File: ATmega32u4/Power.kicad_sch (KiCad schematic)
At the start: 6 parts, among them U1 AMS1117-3.3

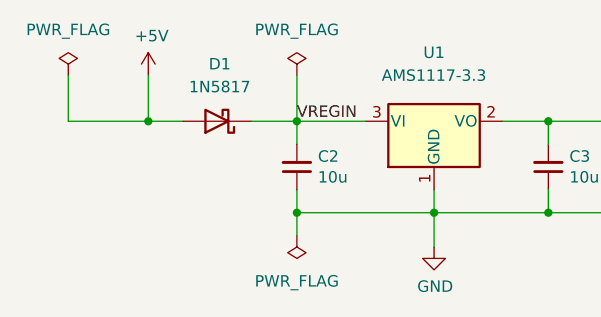
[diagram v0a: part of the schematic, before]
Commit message: Review and updates to power path
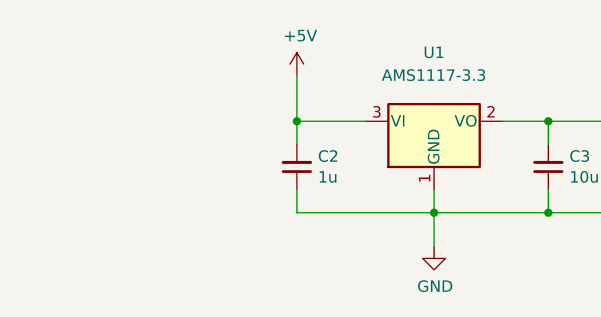
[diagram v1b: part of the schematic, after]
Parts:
- removed D1: 1N5817, Diode_SMD:D_SOD-323, symbol Diode:1N5817
- C2: value 10u -> 1u; footprint Capacitor_SMD:C_0805_2012Metric -> Capacitor_SMD:C_0603_1608Metric
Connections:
- net VREGIN is gone; now on net +5V: C2.2, U1.3 (VI)
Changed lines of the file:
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@@
   (junction (at 163.83 92.71) (diameter 0) (color 0 0 0 0)
-  )
-  (junction (at 127 92.71) (diameter 0) (color 0 0 0 0)
-  )
-  (junction (at 127 102.87) (diameter 0) (color 0 0 0 0)
   )
   (junction (at 163.83 102.87) (diameter 0) (color 0 0 0 0)
   )
-  (junction (at 110.49 92.71) (diameter 0) (color 0 0 0 0)
+  (junction (at 127 92.71) (diameter 0) (color 0 0 0 0)
   )
   (junction (at 154.94 92.71) (diameter 0) (color 0 0 0 0)
@@
     (stroke (width 0) (type default) (color 0 0 0 0))
   )
-  (wire (pts (xy 172.72 95.25) (xy 172.72 92.71))
+  (wire (pts (xy 127 92.71) (xy 127 95.25))
     (stroke (width 0) (type default) (color 0 0 0 0))
   )
-  (wire (pts (xy 127 105.41) (xy 127 102.87))
+  (wire (pts (xy 172.72 95.25) (xy 172.72 92.71))
     (stroke (width 0) (type default) (color 0 0 0 0))
   )
@@
     (stroke (width 0) (type default) (color 0 0 0 0))
   )
+  (wire (pts (xy 127 102.87) (xy 142.24 102.87))
+    (stroke (width 0) (type default) (color 0 0 0 0))
+  )
   (wire (pts (xy 154.94 95.25) (xy 154.94 92.71))
     (stroke (width 0) (type default) (color 0 0 0 0))
   )
-  (wire (pts (xy 127 95.25) (xy 127 92.71))
-    (stroke (width 0) (type default) (color 0 0 0 0))
-  )
   (wire (pts (xy 172.72 100.33) (xy 172.72 102.87))
-    (stroke (width 0) (type default) (color 0 0 0 0))
-  )
-  (wire (pts (xy 114.3 92.71) (xy 110.49 92.71))
-    (stroke (width 0) (type default) (color 0 0 0 0))
-  )
-  (wire (pts (xy 101.6 92.71) (xy 110.49 92.71))
-    (stroke (width 0) (type default) (color 0 0 0 0))
-  )
-  (wire (pts (xy 127 102.87) (xy 142.24 102.87))
     (stroke (width 0) (type default) (color 0 0 0 0))
   )
@@
     (stroke (width 0) (type default) (color 0 0 0 0))
   )
-  (wire (pts (xy 101.6 87.63) (xy 101.6 92.71))
+  (wire (pts (xy 127 100.33) (xy 127 102.87))
     (stroke (width 0) (type default) (color 0 0 0 0))
   )
@@
     (stroke (width 0) (type default) (color 0 0 0 0))
   )
-  (wire (pts (xy 110.49 92.71) (xy 110.49 87.63))
+  (wire (pts (xy 127 92.71) (xy 127 87.63))
     (stroke (width 0) (type default) (color 0 0 0 0))
   )
   (wire (pts (xy 163.83 92.71) (xy 172.72 92.71))
     (stroke (width 0) (type default) (color 0 0 0 0))
-  )
-  (wire (pts (xy 127 100.33) (xy 127 102.87))
-    (stroke (width 0) (type default) (color 0 0 0 0))
-  )
-  (wire (pts (xy 127 87.63) (xy 127 92.71))
-    (stroke (width 0) (type default) (color 0 0 0 0))
-  )
-  (wire (pts (xy 121.92 92.71) (xy 127 92.71))
-    (stroke (width 0) (type default) (color 0 0 0 0))
-  )
-  (label "VREGIN" (at 127 92.71 0)
-    (effects (font (size 1.27 1.27)) (justify left bottom))
   )
   (symbol (lib_id "Device:C_Small") (at 163.83 97.79 180) (unit 1)
@@
     (pin "2")
   )
-  (symbol (lib_id "power:+5V") (at 110.49 87.63 0) (unit 1)
+  (symbol (lib_id "power:+5V") (at 127 87.63 0) (unit 1)
     (in_bom yes) (on_board yes)
-    (property "Reference" "#PWR03" (id 0) (at 110.49 91.44 0)
+    (property "Reference" "#PWR03" (id 0) (at 127 91.44 0)
       (effects (font (size 1.27 1.27)) hide)
     )
-    (property "Value" "+5V" (id 1) (at 110.871 83.2358 0))
-    (property "Footprint" "" (id 2) (at 110.49 87.63 0)
+    (property "Value" "+5V" (id 1) (at 127.381 83.2358 0))
+    (property "Footprint" "" (id 2) (at 127 87.63 0)
       (effects (font (size 1.27 1.27)) hide)
     )
-    (property "Datasheet" "" (id 3) (at 110.49 87.63 0)
-      (effects (font (size 1.27 1.27)) hide)
-    )
-    (pin "1")
-  )
-  (symbol (lib_id "power:PWR_FLAG") (at 101.6 87.63 0) (unit 1)
-    (in_bom yes) (on_board yes) (fields_autoplaced)
-    (property "Reference" "#FLG01" (id 0) (at 101.6 85.725 0)
-      (effects (font (size 1.27 1.27)) hide)
-    )
-    (property "Value" "PWR_FLAG" (id 1) (at 101.6 82.55 0))
-    (property "Footprint" "" (id 2) (at 101.6 87.63 0)
-      (effects (font (size 1.27 1.27)) hide)
-    )
-    (property "Datasheet" "~" (id 3) (at 101.6 87.63 0)
-      (effects (font (size 1.27 1.27)) hide)
-    )
-    (pin "1")
-  )
-  (symbol (lib_id "Device:C_Small") (at 127 97.79 180) (unit 1)
-    (in_bom yes) (on_board yes)
-    (property "Reference" "C2" (id 0) (at 129.3368 96.6216 0)
-      (effects (font (size 1.27 1.27)) (justify right))
-    )
-    (property "Value" "10u" (id 1) (at 129.3368 98.933 0)
-      (effects (font (size 1.27 1.27)) (justify right))
-    )
-    (property "Footprint" "Capacitor_SMD:C_0805_2012Metric" (id 2) (at 127 97.79 0)
-      (effects (font (size 1.27 1.27)) hide)
-    )
-    (property "Datasheet" "~" (id 3) (at 127 97.79 0)
-      (effects (font (size 1.27 1.27)) hide)
-    )
-    (pin "1")
-    (pin "2")
-  )
-  (symbol (lib_id "power:PWR_FLAG") (at 127 105.41 180) (unit 1)
-    (in_bom yes) (on_board yes) (fields_autoplaced)
-    (property "Reference" "#FLG03" (id 0) (at 127 107.315 0)
-      (effects (font (size 1.27 1.27)) hide)
-    )
-    (property "Value" "PWR_FLAG" (id 1) (at 127 110.49 0))
-    (property "Footprint" "" (id 2) (at 127 105.41 0)
-      (effects (font (size 1.27 1.27)) hide)
-    )
-    (property "Datasheet" "~" (id 3) (at 127 105.41 0)
+    (property "Datasheet" "" (id 3) (at 127 87.63 0)
       (effects (font (size 1.27 1.27)) hide)
     )
@@
     (pin "1")
   )
-  (symbol (lib_id "Diode:1N5817") (at 118.11 92.71 180) (unit 1)
-    (in_bom yes) (on_board yes) (fields_autoplaced)
-    (property "Reference" "D1" (id 0) (at 118.4275 86.36 0))
-    (property "Value" "1N5817" (id 1) (at 118.4275 88.9 0))
-    (property "Footprint" "Diode_SMD:D_SOD-323" (id 2) (at 118.11 88.265 0)
-      (effects (font (size 1.27 1.27)) hide)
-    )
-    (property "Datasheet" "http://www.vishay.com/docs/88525/1n5817.pdf" (id 3) (at 118.11 92.71 0)
-      (effects (font (size 1.27 1.27)) hide)
-    )
-    (pin "1")
-    (pin "2")
-  )
   (symbol (lib_id "Regulator_Linear:AMS1117-3.3") (at 142.24 92.71 0) (unit 1)
     (in_bom yes) (on_board yes) (fields_autoplaced)
@@
     (pin "2")
   )
-  (symbol (lib_id "power:PWR_FLAG") (at 127 87.63 0) (unit 1)
-    (in_bom yes) (on_board yes) (fields_autoplaced)
-    (property "Reference" "#FLG02" (id 0) (at 127 85.725 0)
+  (symbol (lib_id "Device:C_Small") (at 127 97.79 180) (unit 1)
+    (in_bom yes) (on_board yes)
+    (property "Reference" "C2" (id 0) (at 129.3368 96.6216 0)
+      (effects (font (size 1.27 1.27)) (justify right))
+    )
+    (property "Value" "1u" (id 1) (at 129.3368 98.933 0)
+      (effects (font (size 1.27 1.27)) (justify right))
+    )
+    (property "Footprint" "Capacitor_SMD:C_0603_1608Metric" (id 2) (at 127 97.79 0)
       (effects (font (size 1.27 1.27)) hide)
     )
-    (property "Value" "PWR_FLAG" (id 1) (at 127 82.55 0))
-    (property "Footprint" "" (id 2) (at 127 87.63 0)
-      (effects (font (size 1.27 1.27)) hide)
-    )
-    (property "Datasheet" "~" (id 3) (at 127 87.63 0)
+    (property "Datasheet" "~" (id 3) (at 127 97.79 0)
       (effects (font (size 1.27 1.27)) hide)
     )
     (pin "1")
+    (pin "2")
   )
 )

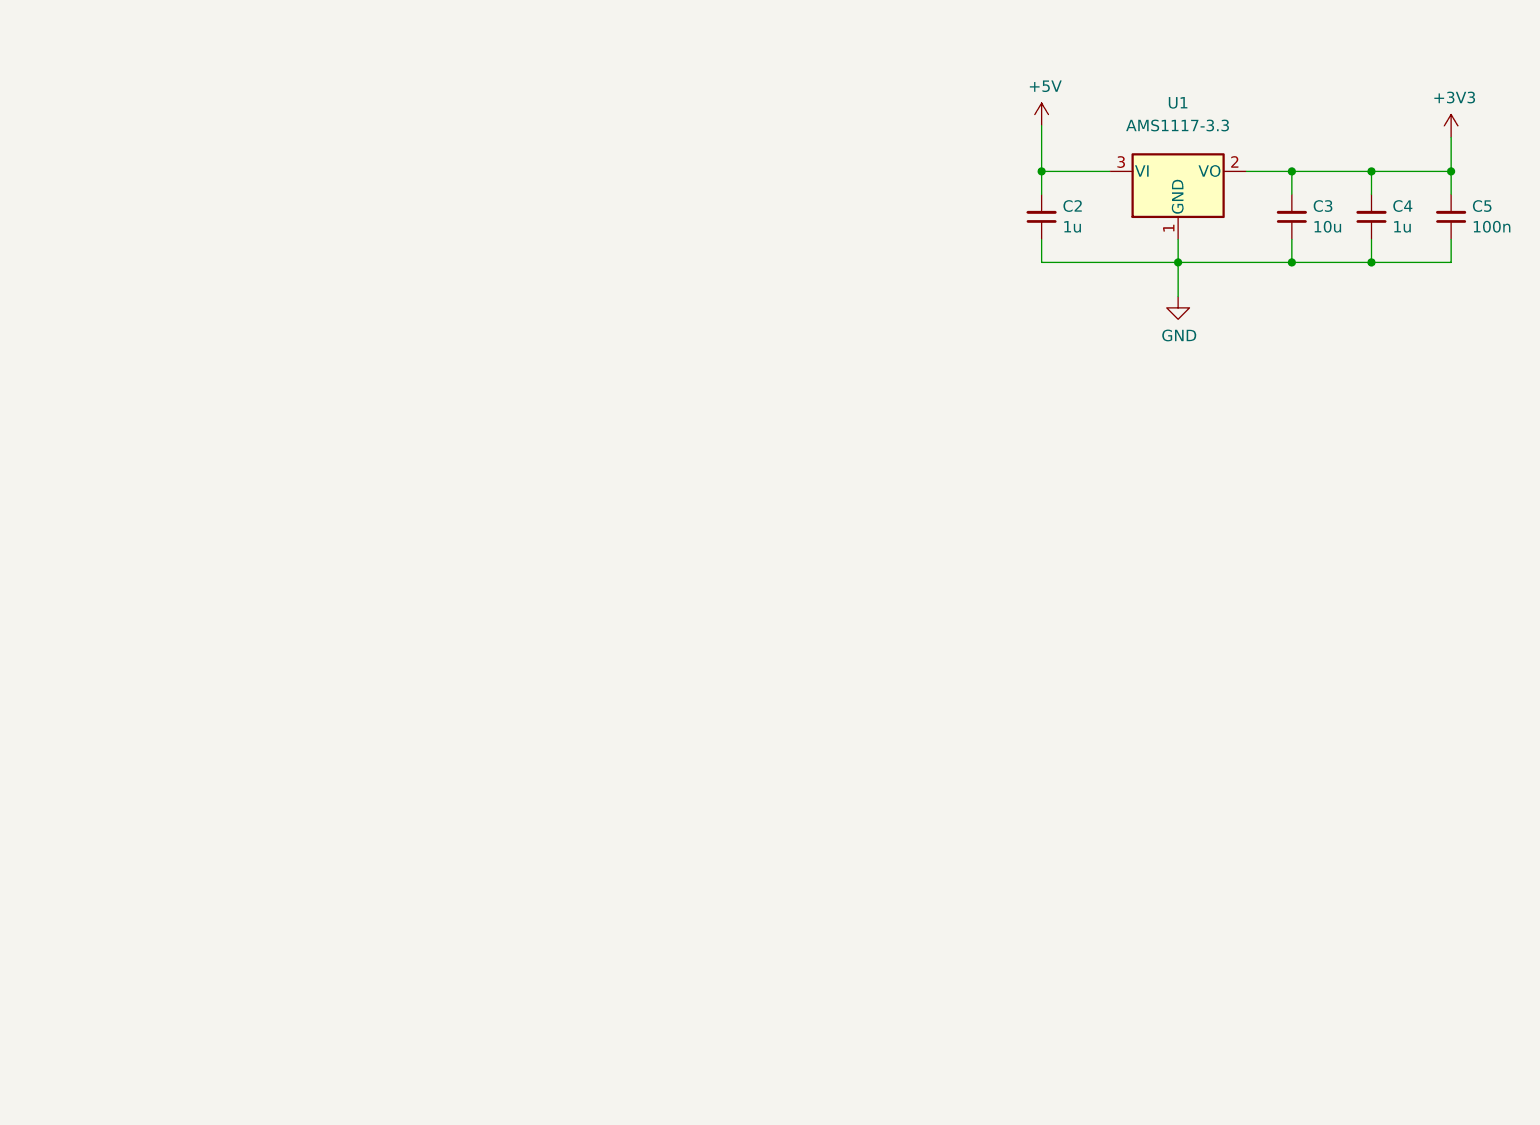
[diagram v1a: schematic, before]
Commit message: Schematic, routing and layout changes post review.
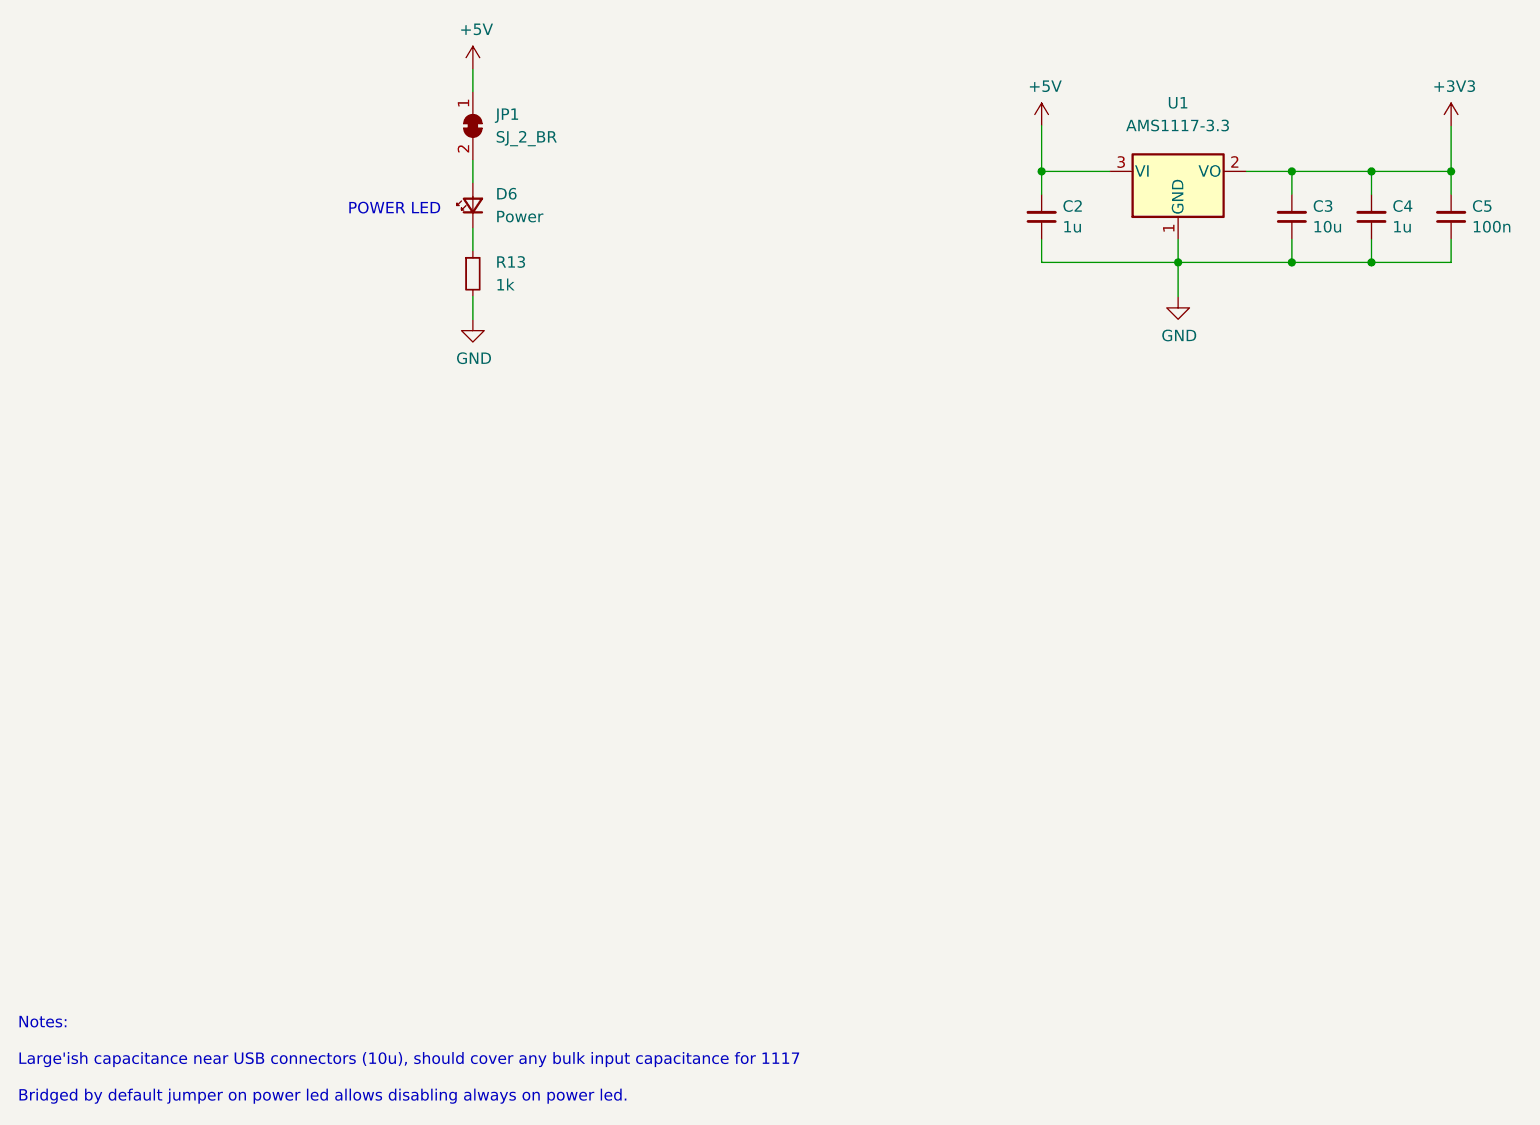
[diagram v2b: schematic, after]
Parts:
- added D6: Power, LED_SMD:LED_0603_1608Metric, symbol Device:LED_Small
- added JP1: SJ_2_BR, Jumper:SolderJumper-2_P1.3mm_Bridged_RoundedPad1.0x1.5mm, symbol Jumper:SolderJumper_2_Bridged
- added R13: 1k, Resistor_SMD:R_0603_1608Metric, symbol Device:R_Small
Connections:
- net +5V: now also JP1.1 (A)
- net GND: now also R13.2
- new net: D6.1 (K), R13.1
- new net: D6.2 (A), JP1.2 (B)
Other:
- note added: "Notes: Large'ish capacitance near USB connectors (10u), should cover any bulk input capacitance for 1117 Bridged by default jumper on power led allows disabling always on power led."
- note added: "POWER LED"
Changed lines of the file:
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@@
     (stroke (width 0) (type default) (color 0 0 0 0))
   )
-  (wire (pts (xy 172.72 92.71) (xy 172.72 88.9))
+  (wire (pts (xy 172.72 92.71) (xy 172.72 87.63))
     (stroke (width 0) (type default) (color 0 0 0 0))
   )
@@
     (stroke (width 0) (type default) (color 0 0 0 0))
   )
+  (wire (pts (xy 63.5 99.06) (xy 63.5 101.6))
+    (stroke (width 0) (type default) (color 0 0 0 0))
+  )
   (wire (pts (xy 154.94 92.71) (xy 163.83 92.71))
     (stroke (width 0) (type default) (color 0 0 0 0))
@@
     (stroke (width 0) (type default) (color 0 0 0 0))
   )
+  (wire (pts (xy 63.5 81.28) (xy 63.5 83.82))
+    (stroke (width 0) (type default) (color 0 0 0 0))
+  )
   (wire (pts (xy 154.94 102.87) (xy 142.24 102.87))
     (stroke (width 0) (type default) (color 0 0 0 0))
@@
     (stroke (width 0) (type default) (color 0 0 0 0))
   )
+  (wire (pts (xy 63.5 91.44) (xy 63.5 93.98))
+    (stroke (width 0) (type default) (color 0 0 0 0))
+  )
   (wire (pts (xy 127 92.71) (xy 127 87.63))
     (stroke (width 0) (type default) (color 0 0 0 0))
@@
     (stroke (width 0) (type default) (color 0 0 0 0))
   )
+  (wire (pts (xy 63.5 106.68) (xy 63.5 109.22))
+    (stroke (width 0) (type default) (color 0 0 0 0))
+  )
+  (text "POWER LED" (at 49.53 97.79 0)
+    (effects (font (size 1.27 1.27)) (justify left bottom))
+  )
+  (text "Notes:\n\nLarge'ish capacitance near USB connectors (10u), should cover any bulk input capacitance for 1117\n\nBridged by default jumper on power led allows disabling always on power led."
+    (at 12.7 196.85 0)
+    (effects (font (size 1.27 1.27)) (justify left bottom))
+  )
   (symbol (lib_id "Device:C_Small") (at 163.83 97.79 180) (unit 1)
     (in_bom yes) (on_board yes)
@@
     )
     (property "Datasheet" "~" (id 3) (at 163.83 97.79 0)
+      (effects (font (size 1.27 1.27)) hide)
+    )
+    (pin "1")
+    (pin "2")
+  )
+  (symbol (lib_id "Device:LED_Small") (at 63.5 96.52 90) (unit 1)
+    (in_bom yes) (on_board yes)
+    (property "Reference" "D6" (id 0) (at 66.04 95.25 90)
+      (effects (font (size 1.27 1.27)) (justify right))
+    )
+    (property "Value" "Power" (id 1) (at 66.04 97.79 90)
+      (effects (font (size 1.27 1.27)) (justify right))
+    )
+    (property "Footprint" "LED_SMD:LED_0603_1608Metric" (id 2) (at 63.5 96.52 90)
+      (effects (font (size 1.27 1.27)) hide)
+    )
+    (property "Datasheet" "~" (id 3) (at 63.5 96.52 90)
       (effects (font (size 1.27 1.27)) hide)
     )
@@
     (pin "1")
   )
+  (symbol (lib_id "power:+5V") (at 63.5 81.28 0) (unit 1)
+    (in_bom yes) (on_board yes)
+    (property "Reference" "#PWR0104" (id 0) (at 63.5 85.09 0)
+      (effects (font (size 1.27 1.27)) hide)
+    )
+    (property "Value" "+5V" (id 1) (at 63.881 76.8858 0))
+    (property "Footprint" "" (id 2) (at 63.5 81.28 0)
+      (effects (font (size 1.27 1.27)) hide)
+    )
+    (property "Datasheet" "" (id 3) (at 63.5 81.28 0)
+      (effects (font (size 1.27 1.27)) hide)
+    )
+    (pin "1")
+  )
+  (symbol (lib_id "Device:R_Small") (at 63.5 104.14 0) (unit 1)
+    (in_bom yes) (on_board yes)
+    (property "Reference" "R13" (id 0) (at 66.04 102.87 0)
+      (effects (font (size 1.27 1.27)) (justify left))
+    )
+    (property "Value" "1k" (id 1) (at 66.04 105.41 0)
+      (effects (font (size 1.27 1.27)) (justify left))
+    )
+    (property "Footprint" "Resistor_SMD:R_0603_1608Metric" (id 2) (at 63.5 104.14 0)
+      (effects (font (size 1.27 1.27)) hide)
+    )
+    (property "Datasheet" "~" (id 3) (at 63.5 104.14 0)
+      (effects (font (size 1.27 1.27)) hide)
+    )
+    (pin "1")
+    (pin "2")
+  )
+  (symbol (lib_id "power:GND") (at 63.5 109.22 0) (unit 1)
+    (in_bom yes) (on_board yes)
+    (property "Reference" "#PWR0103" (id 0) (at 63.5 115.57 0)
+      (effects (font (size 1.27 1.27)) hide)
+    )
+    (property "Value" "GND" (id 1) (at 63.627 113.6142 0))
+    (property "Footprint" "" (id 2) (at 63.5 109.22 0)
+      (effects (font (size 1.27 1.27)) hide)
+    )
+    (property "Datasheet" "" (id 3) (at 63.5 109.22 0)
+      (effects (font (size 1.27 1.27)) hide)
+    )
+    (pin "1")
+  )
+  (symbol (lib_id "Jumper:SolderJumper_2_Bridged") (at 63.5 87.63 270) (unit 1)
+    (in_bom no) (on_board yes)
+    (property "Reference" "JP1" (id 0) (at 66.04 86.36 90)
+      (effects (font (size 1.27 1.27)) (justify left))
+    )
+    (property "Value" "SJ_2_BR" (id 1) (at 66.04 88.9 90)
+      (effects (font (size 1.27 1.27)) (justify left))
+    )
+    (property "Footprint" "Jumper:SolderJumper-2_P1.3mm_Bridged_RoundedPad1.0x1.5mm" (id 2) (at 63.5 87.63 0)
+      (effects (font (size 1.27 1.27)) hide)
+    )
+    (property "Datasheet" "~" (id 3) (at 63.5 87.63 0)
+      (effects (font (size 1.27 1.27)) hide)
+    )
+    (pin "1")
+    (pin "2")
+  )
   (symbol (lib_id "power:GND") (at 142.24 106.68 0) (unit 1)
     (in_bom yes) (on_board yes)
@@
     (pin "1")
   )
-  (symbol (lib_id "power:+3V3") (at 172.72 88.9 0) (unit 1)
-    (in_bom yes) (on_board yes)
-    (property "Reference" "#PWR04" (id 0) (at 172.72 92.71 0)
-      (effects (font (size 1.27 1.27)) hide)
-    )
-    (property "Value" "+3V3" (id 1) (at 173.101 84.5058 0))
-    (property "Footprint" "" (id 2) (at 172.72 88.9 0)
-      (effects (font (size 1.27 1.27)) hide)
-    )
-    (property "Datasheet" "" (id 3) (at 172.72 88.9 0)
-      (effects (font (size 1.27 1.27)) hide)
-    )
+  (symbol (lib_id "power:+3V3") (at 172.72 87.63 0) (unit 1)
+    (in_bom yes) (on_board yes)
+    (property "Reference" "#PWR04" (id 0) (at 172.72 91.44 0)
+      (effects (font (size 1.27 1.27)) hide)
+    )
+    (property "Value" "+3V3" (id 1) (at 173.101 83.2358 0))
+    (property "Footprint" "" (id 2) (at 172.72 87.63 0)
+      (effects (font (size 1.27 1.27)) hide)
+    )
+    (property "Datasheet" "" (id 3) (at 172.72 87.63 0)
+      (effects (font (size 1.27 1.27)) hide)
+    )
